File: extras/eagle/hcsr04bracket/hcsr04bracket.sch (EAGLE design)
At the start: 8 parts, among them J0 J0, J1 J1, J2 J2

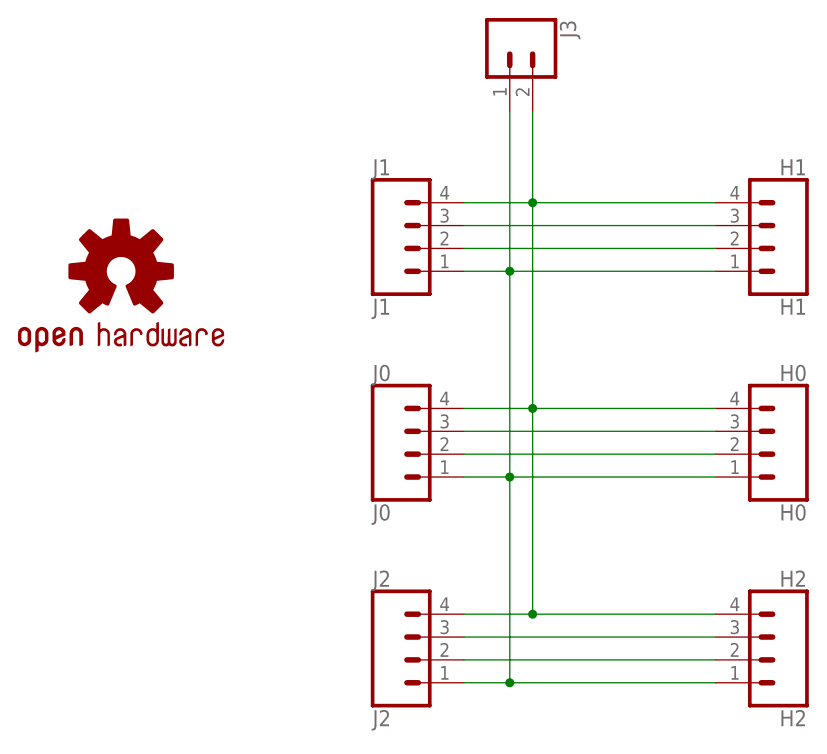
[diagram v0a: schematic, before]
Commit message: Revert "Updates to X2 test and trimount bracket"
This reverts commit f0c77c11ce1398fcc169d7c2890869ee86536cf6.
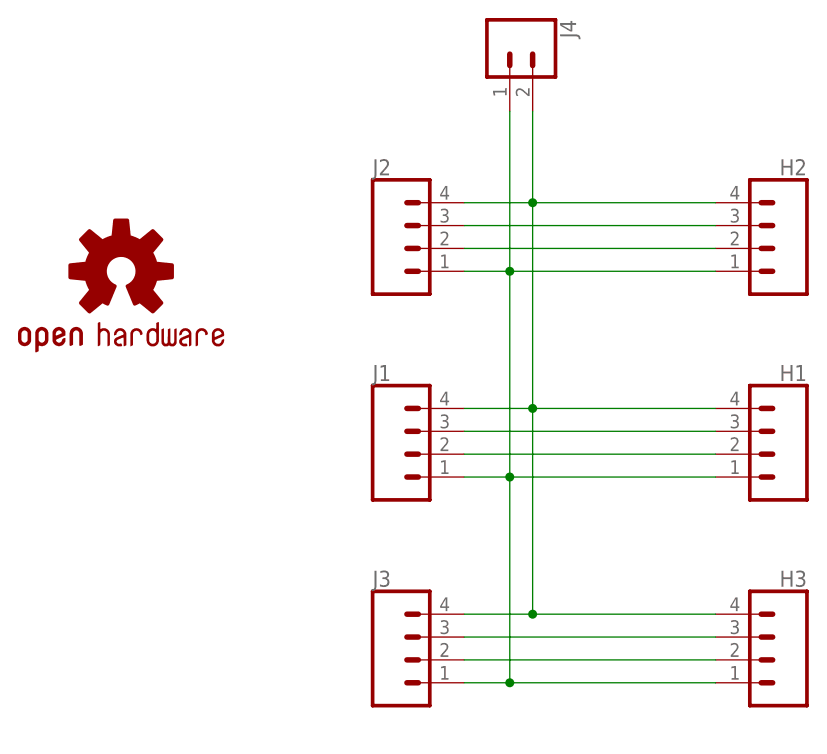
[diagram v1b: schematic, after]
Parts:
- removed H0: H0, mystuff:CONN_04
- removed J0: J0, mystuff:CONN_04
- added H3: (no value), mystuff:CONN_041X04_BSIDE
- added J4: (no value), SparkFun-Connectors:CONN_02
- H1: value H1 -> (none); device mystuff:CONN_04 -> SparkFun-Connectors:CONN_04
- H2: value H2 -> (none); device mystuff:CONN_04 -> SparkFun-Connectors:CONN_04
- J1: value J1 -> (none); device mystuff:CONN_04 -> SparkFun-Connectors:CONN_04
- J2: value J2 -> (none); device mystuff:CONN_04 -> SparkFun-Connectors:CONN_04
- J3: device SparkFun-Connectors:CONN_02 -> SparkFun-Connectors:CONN_04
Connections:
- net E1: now also H2.3, J2.3; no longer H1.3, J1.3
- net E2: now also H1.3, J1.3; no longer H0.3, J0.3
- net E3: now also H3.3, J3.3; no longer H2.3, J2.3
- net GND: now also H3.4, J3.4, J4.2; no longer H0.4, J0.4, J3.2
- net T1: now also H2.2, J2.2; no longer H1.2, J1.2
- net T2: now also H1.2, J1.2; no longer H0.2, J0.2
- net T3: now also H3.2, J3.2; no longer H2.2, J2.2
- net VCC: now also H3.1, J4.1; no longer H0.1, J0.1
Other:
- moved on the sheet: H1, H2, J1, J2
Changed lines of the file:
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@@
 <setting verticaltext="up"/>
 </settings>
-<grid distance="0.1" unitdist="inch" unit="inch" style="lines" multiple="1" display="no" altdistance="0.01" altunitdist="inch" altunit="inch"/>
+<grid distance="0.1" unitdist="inch" unit="inch" style="lines" multiple="1" display="yes" altdistance="0.01" altunitdist="inch" altunit="inch"/>
 <layers>
 <layer number="1" name="Top" color="4" fill="1" visible="no" active="no"/>
@@
 </classes>
 <parts>
-<part name="J1" library="mystuff" deviceset="CONN_04" device="" value="J1"/>
-<part name="J0" library="mystuff" deviceset="CONN_04" device="" value="J0"/>
-<part name="J2" library="mystuff" deviceset="CONN_04" device="" value="J2"/>
-<part name="H1" library="mystuff" deviceset="CONN_04" device="" value="H1"/>
-<part name="H0" library="mystuff" deviceset="CONN_04" device="" value="H0"/>
-<part name="H2" library="mystuff" deviceset="CONN_04" device="" value="H2"/>
-<part name="J3" library="SparkFun-Connectors" deviceset="CONN_02" device=""/>
+<part name="J2" library="SparkFun-Connectors" deviceset="CONN_04" device=""/>
+<part name="J1" library="SparkFun-Connectors" deviceset="CONN_04" device=""/>
+<part name="J3" library="SparkFun-Connectors" deviceset="CONN_04" device=""/>
+<part name="H2" library="SparkFun-Connectors" deviceset="CONN_04" device=""/>
+<part name="H1" library="SparkFun-Connectors" deviceset="CONN_04" device=""/>
+<part name="H3" library="mystuff" deviceset="CONN_04" device="1X04_BSIDE"/>
+<part name="J4" library="SparkFun-Connectors" deviceset="CONN_02" device=""/>
 <part name="LOGO1" library="SparkFun-Aesthetics" deviceset="OSHW-LOGO" device="S" value="OSHW-LOGOS"/>
 </parts>
@@
 </plain>
 <instances>
-<instance part="J1" gate="G$1" x="5.08" y="71.12"/>
-<instance part="J0" gate="G$1" x="5.08" y="48.26"/>
-<instance part="J2" gate="G$1" x="5.08" y="25.4"/>
-<instance part="H1" gate="G$1" x="43.18" y="71.12" rot="MR0"/>
-<instance part="H0" gate="G$1" x="43.18" y="48.26" rot="MR0"/>
-<instance part="H2" gate="G$1" x="43.18" y="25.4" rot="MR0"/>
-<instance part="J3" gate="G$1" x="15.24" y="93.98" rot="R270"/>
+<instance part="J2" gate="G$1" x="5.08" y="71.12"/>
+<instance part="J1" gate="G$1" x="5.08" y="48.26"/>
+<instance part="J3" gate="G$1" x="5.08" y="25.4"/>
+<instance part="H2" gate="G$1" x="43.18" y="71.12" rot="MR0"/>
+<instance part="H1" gate="G$1" x="43.18" y="48.26" rot="MR0"/>
+<instance part="H3" gate="G$1" x="43.18" y="25.4" rot="MR0"/>
+<instance part="J4" gate="G$1" x="15.24" y="93.98" rot="R270"/>
 <instance part="LOGO1" gate="G$1" x="-27.94" y="68.58"/>
 </instances>
@@
 <net name="VCC" class="0">
 <segment>
-<pinref part="H1" gate="G$1" pin="1"/>
-<pinref part="J1" gate="G$1" pin="1"/>
+<pinref part="H2" gate="G$1" pin="1"/>
+<pinref part="J2" gate="G$1" pin="1"/>
 <wire x1="10.16" y1="68.58" x2="15.24" y2="68.58" width="0.1524" layer="91"/>
-<pinref part="J3" gate="G$1" pin="1"/>
+<pinref part="J4" gate="G$1" pin="1"/>
 <wire x1="15.24" y1="68.58" x2="38.1" y2="68.58" width="0.1524" layer="91"/>
 <wire x1="15.24" y1="86.36" x2="15.24" y2="68.58" width="0.1524" layer="91"/>
 <junction x="15.24" y="68.58"/>
-<pinref part="J0" gate="G$1" pin="1"/>
-<pinref part="H0" gate="G$1" pin="1"/>
+<pinref part="J1" gate="G$1" pin="1"/>
+<pinref part="H1" gate="G$1" pin="1"/>
 <wire x1="10.16" y1="45.72" x2="15.24" y2="45.72" width="0.1524" layer="91"/>
 <wire x1="15.24" y1="45.72" x2="38.1" y2="45.72" width="0.1524" layer="91"/>
 <wire x1="15.24" y1="68.58" x2="15.24" y2="45.72" width="0.1524" layer="91"/>
 <junction x="15.24" y="45.72"/>
-<pinref part="H2" gate="G$1" pin="1"/>
-<pinref part="J2" gate="G$1" pin="1"/>
+<pinref part="H3" gate="G$1" pin="1"/>
+<pinref part="J3" gate="G$1" pin="1"/>
 <wire x1="10.16" y1="22.86" x2="15.24" y2="22.86" width="0.1524" layer="91"/>
 <wire x1="15.24" y1="22.86" x2="38.1" y2="22.86" width="0.1524" layer="91"/>
@@
 <net name="E1" class="0">
 <segment>
+<pinref part="J2" gate="G$1" pin="3"/>
+<pinref part="H2" gate="G$1" pin="3"/>
+<wire x1="10.16" y1="73.66" x2="38.1" y2="73.66" width="0.1524" layer="91"/>
+</segment>
+</net>
+<net name="T1" class="0">
+<segment>
+<pinref part="J2" gate="G$1" pin="2"/>
+<pinref part="H2" gate="G$1" pin="2"/>
+<wire x1="10.16" y1="71.12" x2="38.1" y2="71.12" width="0.1524" layer="91"/>
+</segment>
+</net>
+<net name="E2" class="0">
+<segment>
 <pinref part="J1" gate="G$1" pin="3"/>
 <pinref part="H1" gate="G$1" pin="3"/>
-<wire x1="10.16" y1="73.66" x2="38.1" y2="73.66" width="0.1524" layer="91"/>
-</segment>
-</net>
-<net name="T1" class="0">
+<wire x1="10.16" y1="50.8" x2="38.1" y2="50.8" width="0.1524" layer="91"/>
+</segment>
+</net>
+<net name="T2" class="0">
 <segment>
 <pinref part="J1" gate="G$1" pin="2"/>
 <pinref part="H1" gate="G$1" pin="2"/>
-<wire x1="10.16" y1="71.12" x2="38.1" y2="71.12" width="0.1524" layer="91"/>
-</segment>
-</net>
-<net name="E2" class="0">
-<segment>
-<pinref part="J0" gate="G$1" pin="3"/>
-<pinref part="H0" gate="G$1" pin="3"/>
-<wire x1="10.16" y1="50.8" x2="38.1" y2="50.8" width="0.1524" layer="91"/>
-</segment>
-</net>
-<net name="T2" class="0">
-<segment>
-<pinref part="J0" gate="G$1" pin="2"/>
-<pinref part="H0" gate="G$1" pin="2"/>
 <wire x1="10.16" y1="48.26" x2="38.1" y2="48.26" width="0.1524" layer="91"/>
 </segment>
@@
 <net name="E3" class="0">
 <segment>
-<pinref part="J2" gate="G$1" pin="3"/>
-<pinref part="H2" gate="G$1" pin="3"/>
+<pinref part="J3" gate="G$1" pin="3"/>
+<pinref part="H3" gate="G$1" pin="3"/>
 <wire x1="10.16" y1="27.94" x2="38.1" y2="27.94" width="0.1524" layer="91"/>
 </segment>
@@
 <net name="T3" class="0">
 <segment>
-<pinref part="J2" gate="G$1" pin="2"/>
-<pinref part="H2" gate="G$1" pin="2"/>
+<pinref part="J3" gate="G$1" pin="2"/>
+<pinref part="H3" gate="G$1" pin="2"/>
 <wire x1="10.16" y1="25.4" x2="38.1" y2="25.4" width="0.1524" layer="91"/>
 </segment>
@@
 <net name="GND" class="0">
 <segment>
-<pinref part="H1" gate="G$1" pin="4"/>
-<pinref part="J1" gate="G$1" pin="4"/>
+<pinref part="H2" gate="G$1" pin="4"/>
+<pinref part="J2" gate="G$1" pin="4"/>
 <wire x1="10.16" y1="76.2" x2="17.78" y2="76.2" width="0.1524" layer="91"/>
-<pinref part="J3" gate="G$1" pin="2"/>
+<pinref part="J4" gate="G$1" pin="2"/>
 <wire x1="17.78" y1="76.2" x2="38.1" y2="76.2" width="0.1524" layer="91"/>
 <wire x1="17.78" y1="86.36" x2="17.78" y2="76.2" width="0.1524" layer="91"/>
 <junction x="17.78" y="76.2"/>
-<pinref part="J0" gate="G$1" pin="4"/>
-<pinref part="H0" gate="G$1" pin="4"/>
+<pinref part="J1" gate="G$1" pin="4"/>
+<pinref part="H1" gate="G$1" pin="4"/>
 <wire x1="10.16" y1="53.34" x2="17.78" y2="53.34" width="0.1524" layer="91"/>
 <wire x1="17.78" y1="53.34" x2="38.1" y2="53.34" width="0.1524" layer="91"/>
 <wire x1="17.78" y1="76.2" x2="17.78" y2="53.34" width="0.1524" layer="91"/>
 <junction x="17.78" y="53.34"/>
-<pinref part="H2" gate="G$1" pin="4"/>
-<pinref part="J2" gate="G$1" pin="4"/>
+<pinref part="H3" gate="G$1" pin="4"/>
+<pinref part="J3" gate="G$1" pin="4"/>
 <wire x1="10.16" y1="30.48" x2="17.78" y2="30.48" width="0.1524" layer="91"/>
 <wire x1="17.78" y1="30.48" x2="38.1" y2="30.48" width="0.1524" layer="91"/>

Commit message: 1.2.0 eagle files and examples updated
Eagle files updated for OctoSonarX2 and Trimounts to reflect modifications between prototype and production.

OctoSonarX2 - tweaked bypass caps. Rerouted 5V with wider traces.
Examples - tidies up with serial only tests and separate LCD tests.
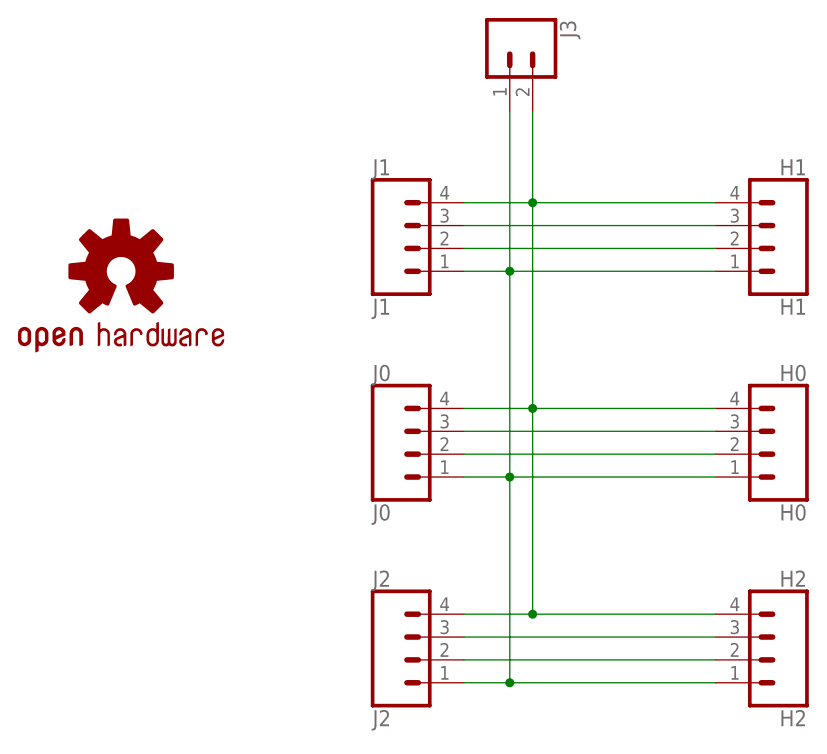
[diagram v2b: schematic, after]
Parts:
- removed H3: (no value), mystuff:CONN_041X04_BSIDE
- removed J4: (no value), SparkFun-Connectors:CONN_02
- added H0: H0, mystuff:CONN_04
- added J0: J0, mystuff:CONN_04
- H1: value (none) -> H1; device SparkFun-Connectors:CONN_04 -> mystuff:CONN_04
- H2: value (none) -> H2; device SparkFun-Connectors:CONN_04 -> mystuff:CONN_04
- J1: value (none) -> J1; device SparkFun-Connectors:CONN_04 -> mystuff:CONN_04
- J2: value (none) -> J2; device SparkFun-Connectors:CONN_04 -> mystuff:CONN_04
- J3: device SparkFun-Connectors:CONN_04 -> SparkFun-Connectors:CONN_02
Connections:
- net E1: now also H1.3, J1.3; no longer H2.3, J2.3
- net E2: now also H0.3, J0.3; no longer H1.3, J1.3
- net E3: now also H2.3, J2.3; no longer H3.3, J3.3
- net GND: now also H0.4, J0.4, J3.2; no longer H3.4, J3.4, J4.2
- net T1: now also H1.2, J1.2; no longer H2.2, J2.2
- net T2: now also H0.2, J0.2; no longer H1.2, J1.2
- net T3: now also H2.2, J2.2; no longer H3.2, J3.2
- net VCC: now also H0.1, J0.1; no longer H3.1, J4.1
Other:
- moved on the sheet: H1, H2, J1, J2
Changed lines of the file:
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@@
 <setting verticaltext="up"/>
 </settings>
-<grid distance="0.1" unitdist="inch" unit="inch" style="lines" multiple="1" display="yes" altdistance="0.01" altunitdist="inch" altunit="inch"/>
+<grid distance="0.1" unitdist="inch" unit="inch" style="lines" multiple="1" display="no" altdistance="0.01" altunitdist="inch" altunit="inch"/>
 <layers>
 <layer number="1" name="Top" color="4" fill="1" visible="no" active="no"/>
@@
 </classes>
 <parts>
-<part name="J2" library="SparkFun-Connectors" deviceset="CONN_04" device=""/>
-<part name="J1" library="SparkFun-Connectors" deviceset="CONN_04" device=""/>
-<part name="J3" library="SparkFun-Connectors" deviceset="CONN_04" device=""/>
-<part name="H2" library="SparkFun-Connectors" deviceset="CONN_04" device=""/>
-<part name="H1" library="SparkFun-Connectors" deviceset="CONN_04" device=""/>
-<part name="H3" library="mystuff" deviceset="CONN_04" device="1X04_BSIDE"/>
-<part name="J4" library="SparkFun-Connectors" deviceset="CONN_02" device=""/>
+<part name="J1" library="mystuff" deviceset="CONN_04" device="" value="J1"/>
+<part name="J0" library="mystuff" deviceset="CONN_04" device="" value="J0"/>
+<part name="J2" library="mystuff" deviceset="CONN_04" device="" value="J2"/>
+<part name="H1" library="mystuff" deviceset="CONN_04" device="" value="H1"/>
+<part name="H0" library="mystuff" deviceset="CONN_04" device="" value="H0"/>
+<part name="H2" library="mystuff" deviceset="CONN_04" device="" value="H2"/>
+<part name="J3" library="SparkFun-Connectors" deviceset="CONN_02" device=""/>
 <part name="LOGO1" library="SparkFun-Aesthetics" deviceset="OSHW-LOGO" device="S" value="OSHW-LOGOS"/>
 </parts>
@@
 </plain>
 <instances>
-<instance part="J2" gate="G$1" x="5.08" y="71.12"/>
-<instance part="J1" gate="G$1" x="5.08" y="48.26"/>
-<instance part="J3" gate="G$1" x="5.08" y="25.4"/>
-<instance part="H2" gate="G$1" x="43.18" y="71.12" rot="MR0"/>
-<instance part="H1" gate="G$1" x="43.18" y="48.26" rot="MR0"/>
-<instance part="H3" gate="G$1" x="43.18" y="25.4" rot="MR0"/>
-<instance part="J4" gate="G$1" x="15.24" y="93.98" rot="R270"/>
+<instance part="J1" gate="G$1" x="5.08" y="71.12"/>
+<instance part="J0" gate="G$1" x="5.08" y="48.26"/>
+<instance part="J2" gate="G$1" x="5.08" y="25.4"/>
+<instance part="H1" gate="G$1" x="43.18" y="71.12" rot="MR0"/>
+<instance part="H0" gate="G$1" x="43.18" y="48.26" rot="MR0"/>
+<instance part="H2" gate="G$1" x="43.18" y="25.4" rot="MR0"/>
+<instance part="J3" gate="G$1" x="15.24" y="93.98" rot="R270"/>
 <instance part="LOGO1" gate="G$1" x="-27.94" y="68.58"/>
 </instances>
@@
 <net name="VCC" class="0">
 <segment>
-<pinref part="H2" gate="G$1" pin="1"/>
-<pinref part="J2" gate="G$1" pin="1"/>
+<pinref part="H1" gate="G$1" pin="1"/>
+<pinref part="J1" gate="G$1" pin="1"/>
 <wire x1="10.16" y1="68.58" x2="15.24" y2="68.58" width="0.1524" layer="91"/>
-<pinref part="J4" gate="G$1" pin="1"/>
+<pinref part="J3" gate="G$1" pin="1"/>
 <wire x1="15.24" y1="68.58" x2="38.1" y2="68.58" width="0.1524" layer="91"/>
 <wire x1="15.24" y1="86.36" x2="15.24" y2="68.58" width="0.1524" layer="91"/>
 <junction x="15.24" y="68.58"/>
-<pinref part="J1" gate="G$1" pin="1"/>
-<pinref part="H1" gate="G$1" pin="1"/>
+<pinref part="J0" gate="G$1" pin="1"/>
+<pinref part="H0" gate="G$1" pin="1"/>
 <wire x1="10.16" y1="45.72" x2="15.24" y2="45.72" width="0.1524" layer="91"/>
 <wire x1="15.24" y1="45.72" x2="38.1" y2="45.72" width="0.1524" layer="91"/>
 <wire x1="15.24" y1="68.58" x2="15.24" y2="45.72" width="0.1524" layer="91"/>
 <junction x="15.24" y="45.72"/>
-<pinref part="H3" gate="G$1" pin="1"/>
-<pinref part="J3" gate="G$1" pin="1"/>
+<pinref part="H2" gate="G$1" pin="1"/>
+<pinref part="J2" gate="G$1" pin="1"/>
 <wire x1="10.16" y1="22.86" x2="15.24" y2="22.86" width="0.1524" layer="91"/>
 <wire x1="15.24" y1="22.86" x2="38.1" y2="22.86" width="0.1524" layer="91"/>
@@
 <net name="E1" class="0">
 <segment>
+<pinref part="J1" gate="G$1" pin="3"/>
+<pinref part="H1" gate="G$1" pin="3"/>
+<wire x1="10.16" y1="73.66" x2="38.1" y2="73.66" width="0.1524" layer="91"/>
+</segment>
+</net>
+<net name="T1" class="0">
+<segment>
+<pinref part="J1" gate="G$1" pin="2"/>
+<pinref part="H1" gate="G$1" pin="2"/>
+<wire x1="10.16" y1="71.12" x2="38.1" y2="71.12" width="0.1524" layer="91"/>
+</segment>
+</net>
+<net name="E2" class="0">
+<segment>
+<pinref part="J0" gate="G$1" pin="3"/>
+<pinref part="H0" gate="G$1" pin="3"/>
+<wire x1="10.16" y1="50.8" x2="38.1" y2="50.8" width="0.1524" layer="91"/>
+</segment>
+</net>
+<net name="T2" class="0">
+<segment>
+<pinref part="J0" gate="G$1" pin="2"/>
+<pinref part="H0" gate="G$1" pin="2"/>
+<wire x1="10.16" y1="48.26" x2="38.1" y2="48.26" width="0.1524" layer="91"/>
+</segment>
+</net>
+<net name="E3" class="0">
+<segment>
 <pinref part="J2" gate="G$1" pin="3"/>
 <pinref part="H2" gate="G$1" pin="3"/>
-<wire x1="10.16" y1="73.66" x2="38.1" y2="73.66" width="0.1524" layer="91"/>
-</segment>
-</net>
-<net name="T1" class="0">
+<wire x1="10.16" y1="27.94" x2="38.1" y2="27.94" width="0.1524" layer="91"/>
+</segment>
+</net>
+<net name="T3" class="0">
 <segment>
 <pinref part="J2" gate="G$1" pin="2"/>
 <pinref part="H2" gate="G$1" pin="2"/>
-<wire x1="10.16" y1="71.12" x2="38.1" y2="71.12" width="0.1524" layer="91"/>
-</segment>
-</net>
-<net name="E2" class="0">
-<segment>
-<pinref part="J1" gate="G$1" pin="3"/>
-<pinref part="H1" gate="G$1" pin="3"/>
-<wire x1="10.16" y1="50.8" x2="38.1" y2="50.8" width="0.1524" layer="91"/>
-</segment>
-</net>
-<net name="T2" class="0">
-<segment>
-<pinref part="J1" gate="G$1" pin="2"/>
-<pinref part="H1" gate="G$1" pin="2"/>
-<wire x1="10.16" y1="48.26" x2="38.1" y2="48.26" width="0.1524" layer="91"/>
-</segment>
-</net>
-<net name="E3" class="0">
-<segment>
-<pinref part="J3" gate="G$1" pin="3"/>
-<pinref part="H3" gate="G$1" pin="3"/>
-<wire x1="10.16" y1="27.94" x2="38.1" y2="27.94" width="0.1524" layer="91"/>
-</segment>
-</net>
-<net name="T3" class="0">
-<segment>
+<wire x1="10.16" y1="25.4" x2="38.1" y2="25.4" width="0.1524" layer="91"/>
+</segment>
+</net>
+<net name="GND" class="0">
+<segment>
+<pinref part="H1" gate="G$1" pin="4"/>
+<pinref part="J1" gate="G$1" pin="4"/>
+<wire x1="10.16" y1="76.2" x2="17.78" y2="76.2" width="0.1524" layer="91"/>
 <pinref part="J3" gate="G$1" pin="2"/>
-<pinref part="H3" gate="G$1" pin="2"/>
-<wire x1="10.16" y1="25.4" x2="38.1" y2="25.4" width="0.1524" layer="91"/>
-</segment>
-</net>
-<net name="GND" class="0">
-<segment>
-<pinref part="H2" gate="G$1" pin="4"/>
-<pinref part="J2" gate="G$1" pin="4"/>
-<wire x1="10.16" y1="76.2" x2="17.78" y2="76.2" width="0.1524" layer="91"/>
-<pinref part="J4" gate="G$1" pin="2"/>
 <wire x1="17.78" y1="76.2" x2="38.1" y2="76.2" width="0.1524" layer="91"/>
 <wire x1="17.78" y1="86.36" x2="17.78" y2="76.2" width="0.1524" layer="91"/>
 <junction x="17.78" y="76.2"/>
-<pinref part="J1" gate="G$1" pin="4"/>
-<pinref part="H1" gate="G$1" pin="4"/>
+<pinref part="J0" gate="G$1" pin="4"/>
+<pinref part="H0" gate="G$1" pin="4"/>
 <wire x1="10.16" y1="53.34" x2="17.78" y2="53.34" width="0.1524" layer="91"/>
 <wire x1="17.78" y1="53.34" x2="38.1" y2="53.34" width="0.1524" layer="91"/>
 <wire x1="17.78" y1="76.2" x2="17.78" y2="53.34" width="0.1524" layer="91"/>
 <junction x="17.78" y="53.34"/>
-<pinref part="H3" gate="G$1" pin="4"/>
-<pinref part="J3" gate="G$1" pin="4"/>
+<pinref part="H2" gate="G$1" pin="4"/>
+<pinref part="J2" gate="G$1" pin="4"/>
 <wire x1="10.16" y1="30.48" x2="17.78" y2="30.48" width="0.1524" layer="91"/>
 <wire x1="17.78" y1="30.48" x2="38.1" y2="30.48" width="0.1524" layer="91"/>
